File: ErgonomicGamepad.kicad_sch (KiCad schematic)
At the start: 84 parts, among them J1 USB_C_Receptacle_USB2.0_16P, J2 Conn_01x08, J3 Conn_01x08, J4 Conn_01x08, J5 AVR-ISP-6, J6 Conn_01x08, J7 1824417, SW01 SW_DIP_x01, SW02 SW_DIP_x01, SW03 SW_DIP_x01, SW04 SW_DIP_x01, SW05 SW_DIP_x01, SW06 SW_DIP_x01, SW07 SW_DIP_x01, SW08 SW_DIP_x01, SW09 SW_DIP_x01, SW10 SW_DIP_x01, SW11 SW_DIP_x01, SW12 SW_DIP_x01, SW13 SW_DIP_x01, SW14 SW_DIP_x01, SW15 SW_DIP_x01, SW16 SW_DIP_x01, SW17 SW_DIP_x01, SW18 SW_DIP_x01, SW19 SW_DIP_x01, SW20 SW_DIP_x01, SW21 SW_DIP_x01, SW22 SW_DIP_x01, SW23 SW_DIP_x01, SW24 SW_DIP_x01, U1 ATmega32U4-A, U2 USBLC6-2SC6, Y1 Crystal

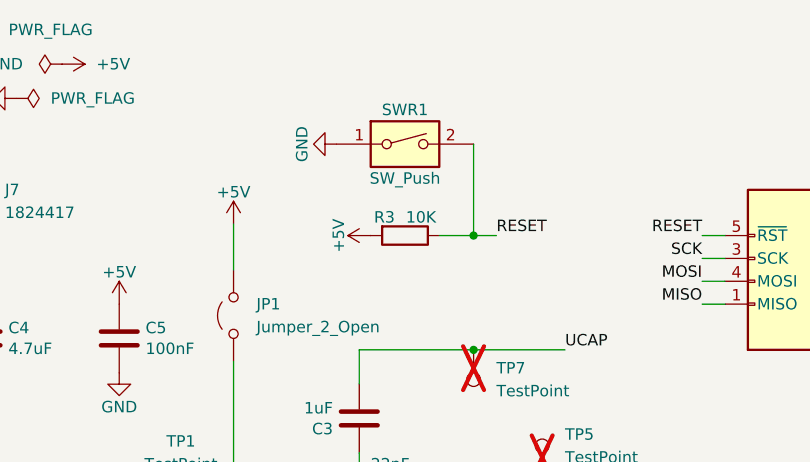
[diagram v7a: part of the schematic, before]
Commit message: schematic: specify SWR1 as Omron B3U-3000P side-actuated switch
SWR1 (reset button) needs to be side-mounted at the board edge and
momentary (not on/off, which would hold RESET low indefinitely).
Went through two candidates before landing here: TS24CA looked
right-angle in text listings but its actual mechanical drawing shows
a top-actuated profile, so it was dropped. Omron B3U-3000P is
confirmed genuinely side-actuated directly from KiCad's own bundled
footprint description ("Side-actuated Model"), and KiCad already
ships a verified footprint for this exact part
(Button_Switch_SMD:SW_SPST_B3U-3000P), so no custom footprint
guessing was needed. LCSC C963349.

Co-Authored-By: Claude Sonnet 5 <noreply@anthropic.com>
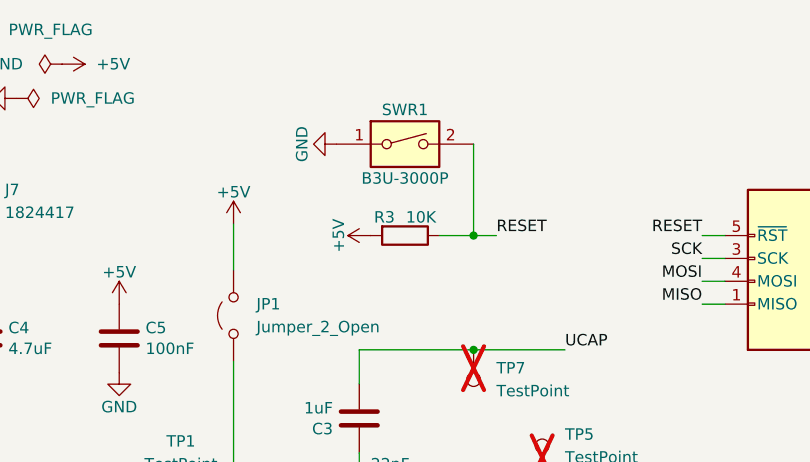
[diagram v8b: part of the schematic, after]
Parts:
- SWR1: value SW_Push -> B3U-3000P; footprint Button_Switch_SMD:SW_SPST_TL3342 -> Button_Switch_SMD:SW_SPST_B3U-3000P; LCSC (none) -> C963349; MPN (none) -> B3U-3000P; Manufacturer (none) -> Omron
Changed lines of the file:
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@@
 			)
 		)
-		(property "Value" "SW_Push"
+		(property "Value" "B3U-3000P"
 			(at 73.66 36.83 0)
 			(show_name no)
@@
 			)
 		)
-		(property "Footprint" "Button_Switch_SMD:SW_SPST_TL3342"
+		(property "Footprint" "Button_Switch_SMD:SW_SPST_B3U-3000P"
 			(at 73.66 33.02 0)
 			(hide yes)
@@
 			)
 		)
-		(property "Datasheet" ""
+		(property "Datasheet" "https://www.lcsc.com/datasheet/C963349.pdf"
 			(at 73.66 33.02 0)
 			(hide yes)
@@
 			)
 		)
-		(property "Manufacturer" ""
+		(property "Manufacturer" "Omron"
 			(at 73.66 33.02 0)
 			(hide yes)
@@
 			)
 		)
-		(property "MPN" ""
+		(property "MPN" "B3U-3000P"
 			(at 73.66 33.02 0)
 			(hide yes)
@@
 			)
 		)
-		(property "LCSC" ""
+		(property "LCSC" "C963349"
 			(at 73.66 33.02 0)
 			(hide yes)
